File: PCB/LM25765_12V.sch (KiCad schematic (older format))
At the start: 8 parts, among them U6 LM2576S-12

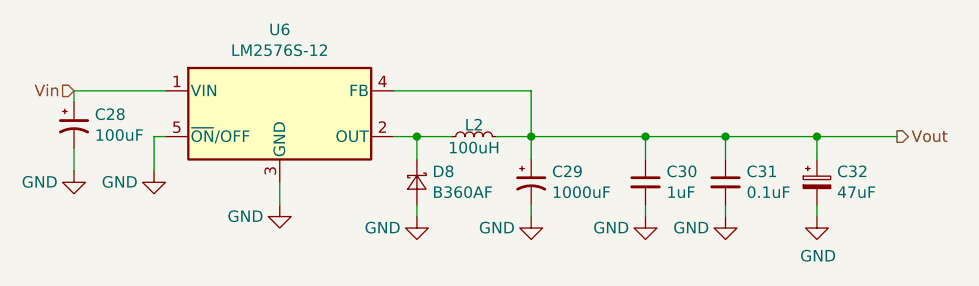
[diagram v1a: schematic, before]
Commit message: Added remaining test points
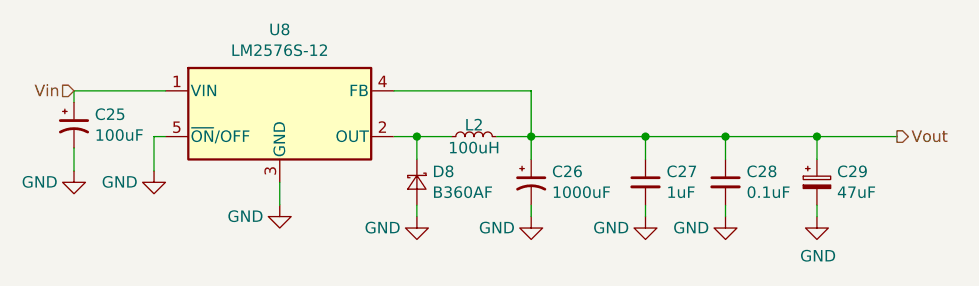
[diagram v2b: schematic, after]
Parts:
- renumbered C28 to C25, C29 to C26, C30 to C27, C31 to C28, C32 to C29, U6 to U8
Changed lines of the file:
@@
 AR Path="/5E880E11/5E904307/5E8CA262" Ref="#PWR?"  Part="1"
 AR Path="/5E880E11/5E9C764B/5E8CA262" Ref="#PWR?"  Part="1"
-AR Path="/5E880E11/5E9C98F5/5E8CA262" Ref="#PWR085"  Part="1"
-F 0 "#PWR085" H 5200 3900 50  0001 C CNN
+AR Path="/5E880E11/5E9C98F5/5E8CA262" Ref="#PWR081"  Part="1"
+F 0 "#PWR081" H 5200 3900 50  0001 C CNN
 F 1 "GND" H 5050 4100 50  0000 C CNN
 F 2 "" H 5200 4150 50  0001 C CNN
@@
 AR Path="/5E880E11/5E904307/5E8CA263" Ref="U?"  Part="1"
 AR Path="/5E880E11/5E9C764B/5E8CA263" Ref="U?"  Part="1"
-AR Path="/5E880E11/5E9C98F5/5E8CA263" Ref="U6"  Part="1"
-F 0 "U6" H 5200 4117 50  0000 C CNN
+AR Path="/5E880E11/5E9C98F5/5E8CA263" Ref="U8"  Part="1"
+F 0 "U8" H 5200 4117 50  0000 C CNN
 F 1 "LM2576S-12" H 5200 4026 50  0000 C CNN
 F 2 "Package_TO_SOT_SMD:TO-263-5_TabPin3" H 5200 3500 50  0001 L CIN
@@
 AR Path="/5E880E11/5E904307/5E8CA264" Ref="C?"  Part="1"
 AR Path="/5E880E11/5E9C764B/5E8CA264" Ref="C?"  Part="1"
-AR Path="/5E880E11/5E9C98F5/5E8CA264" Ref="C29"  Part="1"
-F 0 "C29" H 6391 4096 50  0000 L CNN
+AR Path="/5E880E11/5E9C98F5/5E8CA264" Ref="C26"  Part="1"
+F 0 "C26" H 6391 4096 50  0000 L CNN
 F 1 "1000uF" H 6391 4005 50  0000 L CNN
 F 2 "Capacitor_SMD:CP_Elec_8x10" H 6300 4050 50  0001 C CNN
@@
 AR Path="/5E880E11/5E904307/5E8CA265" Ref="#PWR?"  Part="1"
 AR Path="/5E880E11/5E9C764B/5E8CA265" Ref="#PWR?"  Part="1"
-AR Path="/5E880E11/5E9C98F5/5E8CA265" Ref="#PWR087"  Part="1"
-F 0 "#PWR087" H 6300 3950 50  0001 C CNN
+AR Path="/5E880E11/5E9C98F5/5E8CA265" Ref="#PWR083"  Part="1"
+F 0 "#PWR083" H 6300 3950 50  0001 C CNN
 F 1 "GND" H 6150 4150 50  0000 C CNN
 F 2 "" H 6300 4200 50  0001 C CNN
@@
 AR Path="/5E880E11/5E904307/5E8CA267" Ref="#PWR?"  Part="1"
 AR Path="/5E880E11/5E9C764B/5E8CA267" Ref="#PWR?"  Part="1"
-AR Path="/5E880E11/5E9C98F5/5E8CA267" Ref="#PWR086"  Part="1"
-F 0 "#PWR086" H 5800 3950 50  0001 C CNN
+AR Path="/5E880E11/5E9C98F5/5E8CA267" Ref="#PWR082"  Part="1"
+F 0 "#PWR082" H 5800 3950 50  0001 C CNN
 F 1 "GND" H 5650 4150 50  0000 C CNN
 F 2 "" H 5800 4200 50  0001 C CNN
@@
 AR Path="/5E880E11/5E904307/5E8CA26C" Ref="C?"  Part="1"
 AR Path="/5E880E11/5E9C764B/5E8CA26C" Ref="C?"  Part="1"
-AR Path="/5E880E11/5E9C98F5/5E8CA26C" Ref="C30"  Part="1"
-F 0 "C30" H 6892 4096 50  0000 L CNN
+AR Path="/5E880E11/5E9C98F5/5E8CA26C" Ref="C27"  Part="1"
+F 0 "C27" H 6892 4096 50  0000 L CNN
 F 1 "1uF" H 6892 4005 50  0000 L CNN
 F 2 "Capacitors:0603" H 6800 4050 50  0001 C CNN
@@
 AR Path="/5E880E11/5E904307/5E8CA26D" Ref="C?"  Part="1"
 AR Path="/5E880E11/5E9C764B/5E8CA26D" Ref="C?"  Part="1"
-AR Path="/5E880E11/5E9C98F5/5E8CA26D" Ref="C31"  Part="1"
-F 0 "C31" H 7242 4096 50  0000 L CNN
+AR Path="/5E880E11/5E9C98F5/5E8CA26D" Ref="C28"  Part="1"
+F 0 "C28" H 7242 4096 50  0000 L CNN
 F 1 "0.1uF" H 7242 4005 50  0000 L CNN
 F 2 "Capacitors:0603" H 7150 4050 50  0001 C CNN
@@
 AR Path="/5E880E11/5E904307/5B9CEE03" Ref="#PWR?"  Part="1"
 AR Path="/5E880E11/5E9C764B/5B9CEE03" Ref="#PWR?"  Part="1"
-AR Path="/5E880E11/5E9C98F5/5B9CEE03" Ref="#PWR090"  Part="1"
-F 0 "#PWR090" H 7550 3950 50  0001 C CNN
+AR Path="/5E880E11/5E9C98F5/5B9CEE03" Ref="#PWR086"  Part="1"
+F 0 "#PWR086" H 7550 3950 50  0001 C CNN
 F 1 "GND" H 7555 4027 50  0000 C CNN
 F 2 "" H 7550 4200 50  0001 C CNN
@@
 AR Path="/5E880E11/5E904307/5B9CEE1A" Ref="C?"  Part="1"
 AR Path="/5E880E11/5E9C764B/5B9CEE1A" Ref="C?"  Part="1"
-AR Path="/5E880E11/5E9C98F5/5B9CEE1A" Ref="C32"  Part="1"
-F 0 "C32" H 7638 4096 50  0000 L CNN
+AR Path="/5E880E11/5E9C98F5/5B9CEE1A" Ref="C29"  Part="1"
+F 0 "C29" H 7638 4096 50  0000 L CNN
 F 1 "47uF" H 7638 4005 50  0000 L CNN
 F 2 "Capacitor_SMD:CP_Elec_4x5.4" H 7550 4050 50  0001 C CNN
@@
 AR Path="/5E880E11/5E904307/5B9D0690" Ref="#PWR?"  Part="1"
 AR Path="/5E880E11/5E9C764B/5B9D0690" Ref="#PWR?"  Part="1"
-AR Path="/5E880E11/5E9C98F5/5B9D0690" Ref="#PWR088"  Part="1"
-F 0 "#PWR088" H 6800 3950 50  0001 C CNN
+AR Path="/5E880E11/5E9C98F5/5B9D0690" Ref="#PWR084"  Part="1"
+F 0 "#PWR084" H 6800 3950 50  0001 C CNN
 F 1 "GND" H 6650 4150 50  0000 C CNN
 F 2 "" H 6800 4200 50  0001 C CNN
@@
 AR Path="/5E880E11/5E904307/5B9D06AF" Ref="#PWR?"  Part="1"
 AR Path="/5E880E11/5E9C764B/5B9D06AF" Ref="#PWR?"  Part="1"
-AR Path="/5E880E11/5E9C98F5/5B9D06AF" Ref="#PWR089"  Part="1"
-F 0 "#PWR089" H 7150 3950 50  0001 C CNN
+AR Path="/5E880E11/5E9C98F5/5B9D06AF" Ref="#PWR085"  Part="1"
+F 0 "#PWR085" H 7150 3950 50  0001 C CNN
 F 1 "GND" H 7000 4150 50  0000 C CNN
 F 2 "" H 7150 4200 50  0001 C CNN
@@
 AR Path="/5E880E11/5E904307/5B713FC7" Ref="#PWR?"  Part="1"
 AR Path="/5E880E11/5E9C764B/5B713FC7" Ref="#PWR?"  Part="1"
-AR Path="/5E880E11/5E9C98F5/5B713FC7" Ref="#PWR084"  Part="1"
-F 0 "#PWR084" H 4650 3750 50  0001 C CNN
+AR Path="/5E880E11/5E9C98F5/5B713FC7" Ref="#PWR080"  Part="1"
+F 0 "#PWR080" H 4650 3750 50  0001 C CNN
 F 1 "GND" H 4500 3950 50  0000 C CNN
 F 2 "" H 4650 4000 50  0001 C CNN
@@
 AR Path="/5E880E11/5E904307/5B713FD6" Ref="#PWR?"  Part="1"
 AR Path="/5E880E11/5E9C764B/5B713FD6" Ref="#PWR?"  Part="1"
-AR Path="/5E880E11/5E9C98F5/5B713FD6" Ref="#PWR083"  Part="1"
-F 0 "#PWR083" H 4300 3750 50  0001 C CNN
+AR Path="/5E880E11/5E9C98F5/5B713FD6" Ref="#PWR079"  Part="1"
+F 0 "#PWR079" H 4300 3750 50  0001 C CNN
 F 1 "GND" H 4150 3950 50  0000 C CNN
 F 2 "" H 4300 4000 50  0001 C CNN
@@
 AR Path="/5E880E11/5E904307/5B713FCF" Ref="C?"  Part="1"
 AR Path="/5E880E11/5E9C764B/5B713FCF" Ref="C?"  Part="1"
-AR Path="/5E880E11/5E9C98F5/5B713FCF" Ref="C28"  Part="1"
-F 0 "C28" H 4391 3846 50  0000 L CNN
+AR Path="/5E880E11/5E9C98F5/5B713FCF" Ref="C25"  Part="1"
+F 0 "C25" H 4391 3846 50  0000 L CNN
 F 1 "100uF" H 4391 3755 50  0000 L CNN
 F 2 "Capacitor_SMD:CP_Elec_5x5.4" H 4300 3800 50  0001 C CNN

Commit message: Added majority footprints
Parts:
- C27, C28: footprint Capacitors:0603 -> Capacitor_SMD:C_0603_1608Metric
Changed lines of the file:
@@
 F 0 "C27" H 6892 4096 50  0000 L CNN
 F 1 "1uF" H 6892 4005 50  0000 L CNN
-F 2 "Capacitors:0603" H 6800 4050 50  0001 C CNN
+F 2 "Capacitor_SMD:C_0603_1608Metric" H 6800 4050 50  0001 C CNN
 F 3 "" H 6800 4050 50  0001 C CNN
 F 4 "Power Supply" H 6800 4050 50  0001 C CNN "Functional Block"
@@
 F 0 "C28" H 7242 4096 50  0000 L CNN
 F 1 "0.1uF" H 7242 4005 50  0000 L CNN
-F 2 "Capacitors:0603" H 7150 4050 50  0001 C CNN
+F 2 "Capacitor_SMD:C_0603_1608Metric" H 7150 4050 50  0001 C CNN
 F 3 "" H 7150 4050 50  0001 C CNN
 F 4 "Power Supply" H 7150 4050 50  0001 C CNN "Functional Block"

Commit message: Added correct Alu cap MPNs
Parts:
- C25: MPN EEE-1AA101SP -> EEE-FT1C101AR
- C26: MPN UWT0J102MNL1GS -> EEE-FT1C102AP; Manufacturer (none) -> Panasonic
- C29: MPN EEE-0JA470WR -> EEE-1CA470WR
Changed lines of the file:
@@
 F 2 "Capacitor_SMD:CP_Elec_8x10" H 6300 4050 50  0001 C CNN
 F 3 "" H 6300 4050 50  0001 C CNN
-F 4 "UWT0J102MNL1GS" H 6300 4050 50  0001 C CNN "MPN"
+F 4 "EEE-FT1C102AP" H 6300 4050 50  0001 C CNN "MPN"
 F 5 "Power Supply" H 6300 4050 50  0001 C CNN "Functional Block"
 F 6 "Aluminium Film" H -700 -100 50  0001 C CNN "Dielectric"
@@
 F 8 "General Purpose" H -700 -100 50  0001 C CNN "Impedance"
 F 9 "1000hr @ 85degC" H -700 -100 50  0001 C CNN "Lifetime @ Temperature"
+F 10 "Panasonic" H 6300 4050 50  0001 C CNN "Manufacturer"
 	1    6300 4050
 	1    0    0    -1
@@
 F 2 "Capacitor_SMD:CP_Elec_4x5.4" H 7550 4050 50  0001 C CNN
 F 3 "" H 7550 4050 50  0001 C CNN
-F 4 "EEE-0JA470WR" H -700 -100 50  0001 C CNN "MPN"
+F 4 "EEE-1CA470WR" H -700 -100 50  0001 C CNN "MPN"
 F 5 "Panasonic" H -700 -100 50  0001 C CNN "Manufacturer"
 F 6 "Power Supply" H 7550 4050 50  0001 C CNN "Functional Block"
@@
 F 2 "Capacitor_SMD:CP_Elec_5x5.4" H 4300 3800 50  0001 C CNN
 F 3 "" H 4300 3800 50  0001 C CNN
-F 4 "EEE-1AA101SP" H 0   0   50  0001 C CNN "MPN"
+F 4 "EEE-FT1C101AR" H 0   0   50  0001 C CNN "MPN"
 F 5 "Panasonic" H 0   0   50  0001 C CNN "Manufacturer"
 F 6 "Power Supply" H 4300 3800 50  0001 C CNN "Functional Block"
